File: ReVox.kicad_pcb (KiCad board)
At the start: 2 copper layers, 60.8 x 89.2 mm, 41 parts, among them CN1 EXPANSION_PORT, U1 GAL20V8, U2 74LS273, U3 LM386

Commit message: RIP
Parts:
- removed C6: 100n, Capacitor_THT:C_Disc_D7.0mm_W2.5mm_P5.00mm
- added CN2: AUDIO_OUT, ReVox:AudioJack_SJ1-3525N, F.Cu at (145.3, 62.4)
- added CN3: AUDIO_OUT, ReVox:AudioJack_SJ1-3525N, F.Cu at (129.4, 62.4)
- added J1: CONN_SIGNALS, ReVox:PinHeader_2x25_P1.27mm_Vertical, F.Cu at (136.9, 135.3)
- V0: moved to B.Cu
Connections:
- CN1 pad 10: Net-(CN1-Pad10) -> /~cs0
- CN1 pad 11: Net-(CN1-Pad11) -> /~cas
- CN1 pad 12: Net-(CN1-Pad12) -> /mux
- CN1 pad 13: Net-(CN1-Pad13) -> /ba
- CN1 pad 22: Net-(CN1-Pad22) -> /aec
- CN1 pad 4: Net-(CN1-Pad4) -> /~irq
- CN1 pad 6: Net-(CN1-Pad6) -> /c1hi
- CN1 pad 7: Net-(CN1-Pad7) -> /c2lo
- CN1 pad 8: Net-(CN1-Pad8) -> /c2hi
- CN1 pad 9: Net-(CN1-Pad9) -> /~cs1
- CN1 pad AA: Net-(CN1-PadAA) -> /aa
- CN1 pad B: Net-(CN1-PadB) -> /c1lo
- CN1 pad BB: Net-(CN1-PadBB) -> /bb
- CN1 pad D: Net-(CN1-PadD) -> /~ras
- CN1 pad E: Net-(CN1-PadE) -> /phi0
- CN1 pad Z: Net-(CN1-PadZ) -> /z
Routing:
- net +5V: track 0.00 -> 58.5 mm
- net /a9: track 0.00 -> 22.9 mm
- net /a10: track 0.00 -> 20.7 mm
- net /a11: track 0.00 -> 19.7 mm
- net /a12: track 0.00 -> 18.8 mm
- net /a15: track 0.00 -> 18.3 mm
- net /a14: track 0.00 -> 18.3 mm
- net /a13: track 0.00 -> 18.1 mm
- net /phi2: track 0.00 -> 17.0 mm
- net /~reset: track 0.00 -> 16.1 mm
- net /~ras: track 0.00 -> 15.7 mm
- net /c1lo: track 0.00 -> 15.5 mm
- net /phi0: track 0.00 -> 15.0 mm
- net /ext_audio: track 0.00 -> 13.5 mm
- net /~irq: track 0.00 -> 13.0 mm
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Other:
- net class Default: trace_width 0.25 -> 0.2
- board text added: "V1"
- board text removed: "V2"

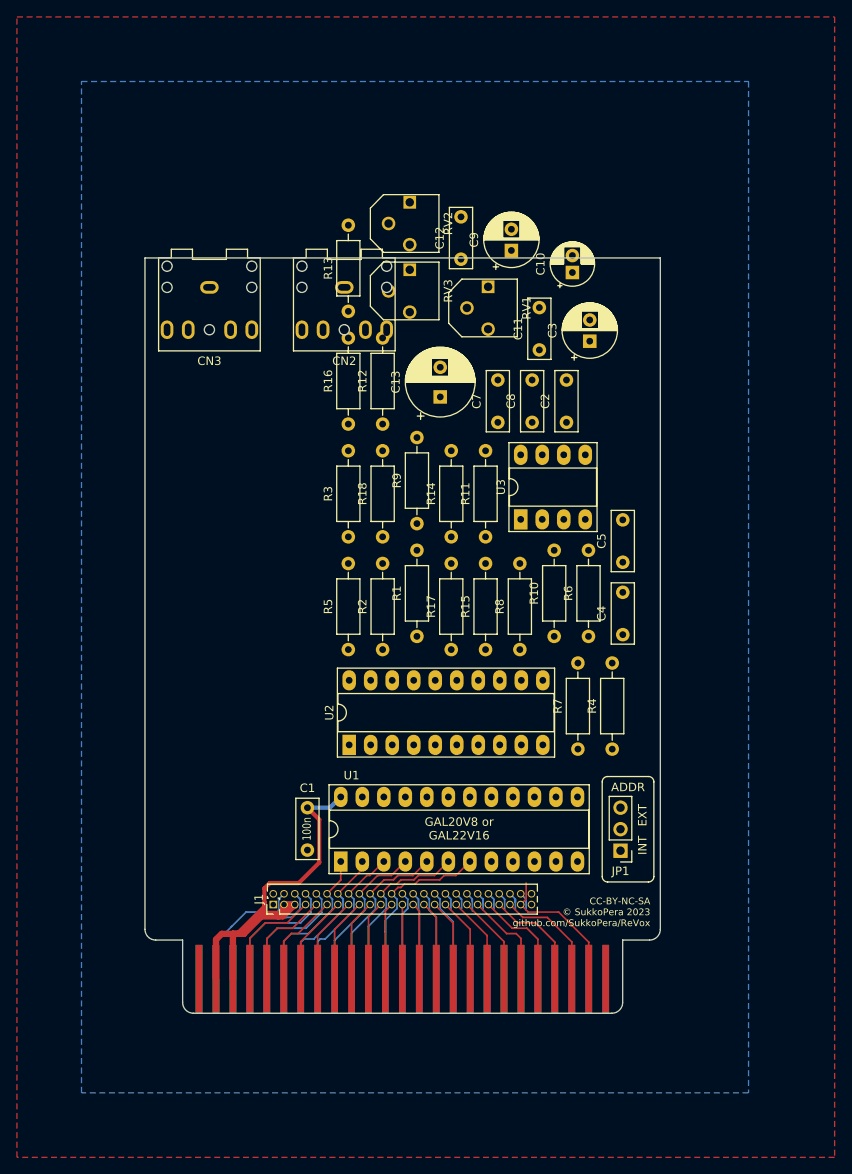
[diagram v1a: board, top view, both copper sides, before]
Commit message: First routing pass completed
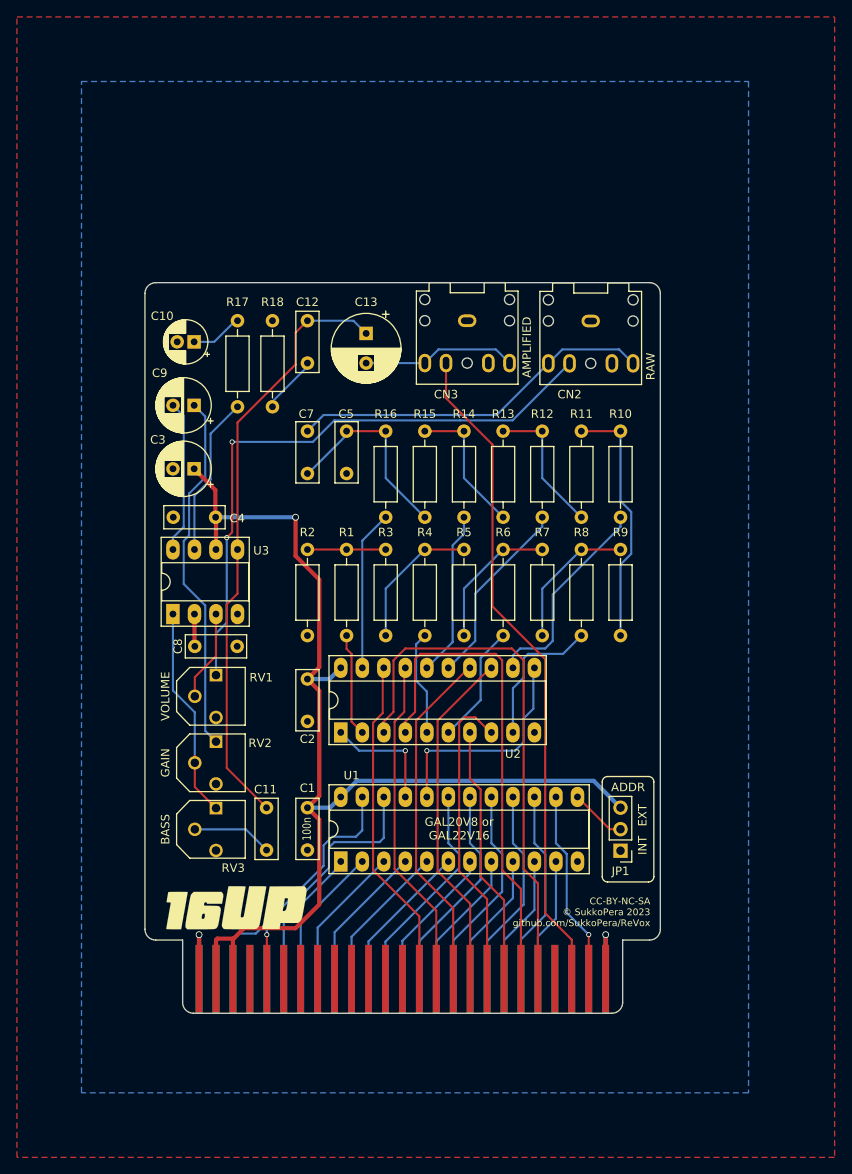
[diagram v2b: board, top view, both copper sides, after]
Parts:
- removed J1: CONN_SIGNALS, ReVox:PinHeader_2x25_P1.27mm_Vertical
- V0: moved to F.Cu
- moved RV2 67.6 mm to (128.9, 118.5)
- moved RV3 67.5 mm to (128.9, 126.4)
- moved C11 62.9 mm to (136.1, 123.8), turned to 270 degrees
- moved RV1 56.0 mm to (128.9, 110.7)
- moved C4 50.0 mm to (130.1, 89.5), turned to 180 degrees
- moved C3 49.1 mm to (127.6, 83.8), turned to 180 degrees
- moved R17 46.3 mm to (132.7, 66.3), turned to 270 degrees
- moved C10 45.4 mm to (127.6, 68.8), turned to 180 degrees
- moved C8 43.7 mm to (132.7, 104.8), turned to 180 degrees
- moved C2 43.0 mm to (141.0, 108.6), turned to 270 degrees
- moved U3 42.5 mm to (125.1, 101.0)
- moved C9 41.7 mm to (127.6, 76.3), turned to 180 degrees
- moved C5 34.2 mm to (145.6, 84.4)
- moved CN3 30.7 mm to (159.8, 66.3)
- moved R13 30.4 mm to (164.1, 89.5)
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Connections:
- C8 pad 2: Net-(C8-Pad2) -> GND
- U1 pad 10: /a6 -> /a2
- U1 pad 11: /a5 -> /a0
- U1 pad 13: /a4 -> Net-(JP1-Pad2)
- U1 pad 14: Net-(JP1-Pad2) -> /phi2
- U1 pad 15: /a3 -> /a1
- U1 pad 16: /a2 -> /a3
- U1 pad 17: /a1 -> /a5
- U1 pad 18: /a0 -> /a7
- U1 pad 19: /~reset -> /a9
- U1 pad 20: /r_~w -> /latch_clk
- U1 pad 22: /latch_clk -> /r_~w
- U1 pad 23: /phi2 -> /~reset
- U1 pad 7: /a9 -> /a8
- U1 pad 8: /a8 -> /a6
- U1 pad 9: /a7 -> /a4
- U3 pad 2: Net-(C8-Pad2) -> GND
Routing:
- net +5V: track 58.5 -> 136.3 mm, vias 0 -> 1
- net /amplifier_in: track 0.00 -> 72.0 mm, vias 0 -> 2
- net Net-(C11-Pad1): track 0.00 -> 70.9 mm
- net /ext_audio: track 13.5 -> 79.4 mm
- net /d0: track 12.2 -> 63.8 mm
- net /d1: track 11.5 -> 58.5 mm
- net /analog_audio: track 0.00 -> 43.1 mm
- net Net-(C9-Pad1): track 0.00 -> 42.9 mm
- net /d5: track 9.67 -> 41.1 mm
- net /d4: track 9.97 -> 40.9 mm
- net /d7: track 9.07 -> 39.4 mm
- net /d6: track 9.37 -> 39.2 mm
- net Net-(R10-Pad2): track 0.00 -> 29.8 mm
- net /latch_clk: track 0.00 -> 26.5 mm, vias 0 -> 1
- net /d3: track 10.3 -> 36.3 mm
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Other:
- board size 60.8 x 89.2 mm -> 60.8 x 86.2 mm
- net class Default: trace_width 0.2 -> 0.25
- board text added: "AMPLIFIED"
- board text added: "BASS"
- board text added: "GAIN"
- board text added: "RAW"
- board text added: "VOLUME"

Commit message: Refinements
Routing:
- net Net-(RV2-Pad2): track 25.8 -> 32.5 mm
- net Net-(C11-Pad1): track 70.9 -> 73.6 mm
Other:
- outline, holes or cut-outs redrawn
- board text added: "2R"
- board text added: "R"

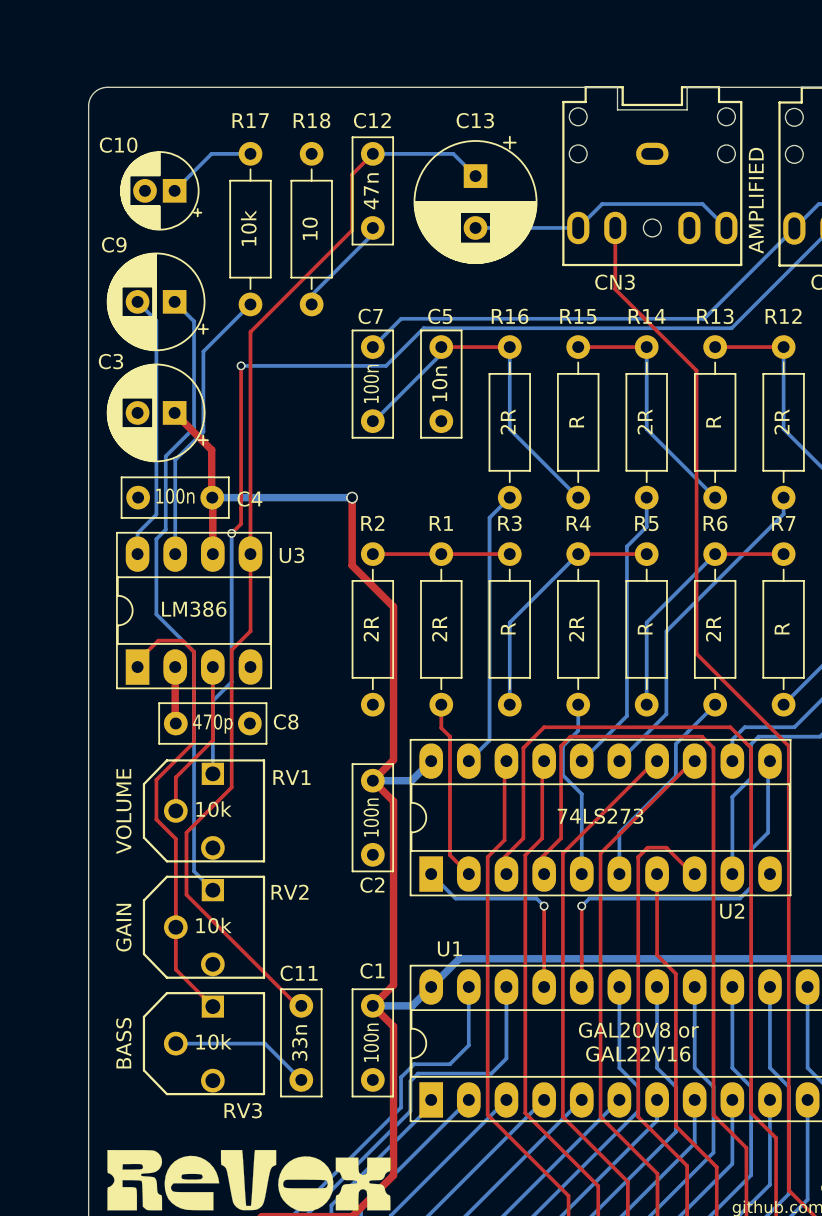
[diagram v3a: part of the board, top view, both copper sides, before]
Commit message: Move pots up, so that they remain accessible while the board is plugged into the machine
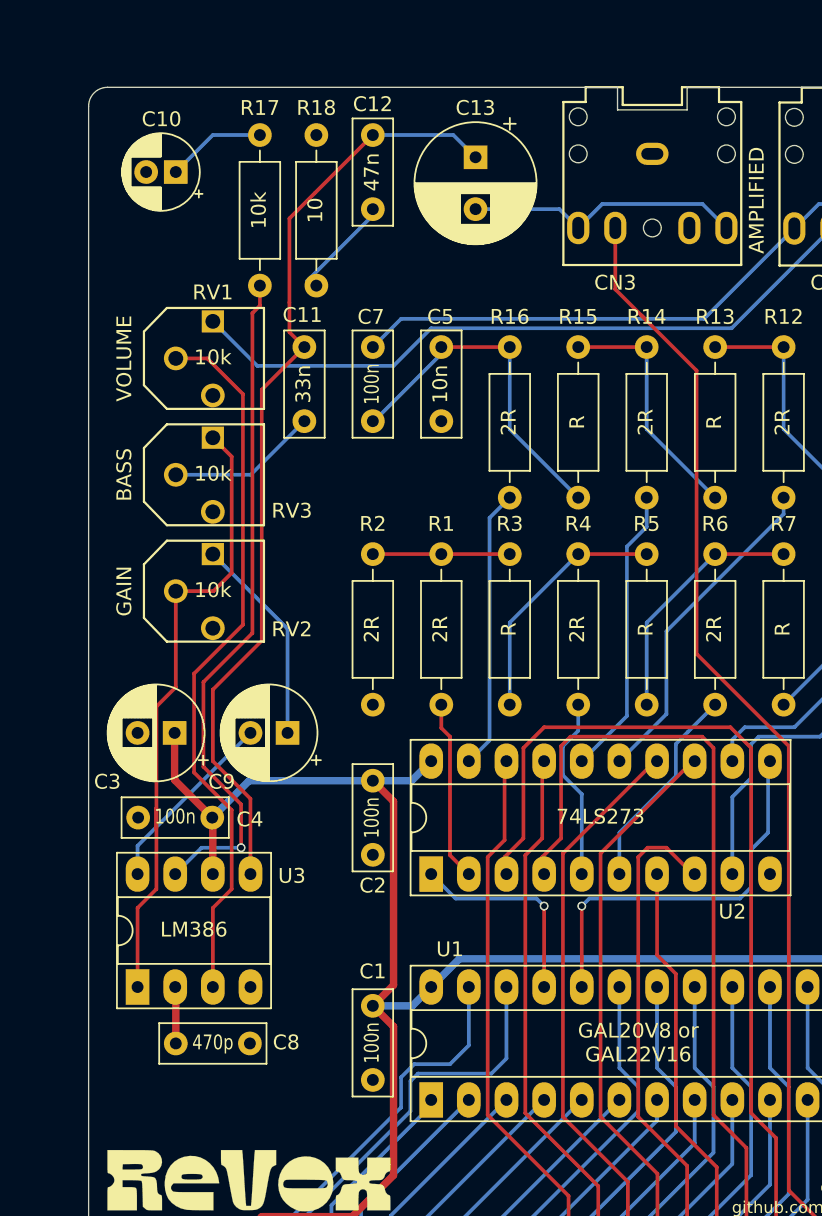
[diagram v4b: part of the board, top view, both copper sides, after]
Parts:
- moved C11 44.5 mm to (136.4, 79.4)
- moved RV3 38.4 mm to (128.9, 88.0)
- moved RV1 30.5 mm to (128.9, 80.1)
- moved C9 30.1 mm to (135.2, 105.4)
- moved RV2 22.7 mm to (128.9, 95.8)
- moved C3 21.6 mm to (127.6, 105.4)
- moved C4 21.6 mm to (130.1, 111.1)
- moved U3 21.6 mm to (125.1, 122.6)
- moved C8 21.6 mm to (132.7, 126.4)
- moved R17 1.42 mm to (133.3, 65.1)
- moved R18 1.31 mm to (137.2, 65.1)
- moved C10 1.27 mm to (127.7, 67.6)
- moved C12 1.27 mm to (141.0, 65.1)
- moved C13 1.27 mm to (147.9, 66.6)
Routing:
- net Net-(RV1-Pad2): track 10.7 -> 48.5 mm
- net Net-(C9-Pad1): track 42.9 -> 14.2 mm
- net Net-(R17-Pad2): track 19.0 -> 45.7 mm, vias 0 -> 1
- net /amplifier_in: track 72.0 -> 46.8 mm, vias 2 -> 0
- net +5V: track 136.3 -> 117.9 mm, vias 1 -> 0
- net Net-(RV2-Pad2): track 32.5 -> 43.1 mm
- net Net-(C11-Pad1): track 73.6 -> 63.8 mm
- net Net-(C9-Pad2): track 18.1 -> 12.7 mm
- net Net-(C11-Pad2): track 9.48 -> 10.2 mm
- net Net-(C10-Pad1): track 6.15 -> 6.71 mm
- net /amplified_audio: track 18.3 -> 18.8 mm

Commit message: Tidy up
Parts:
- moved C12 19.9 mm to (136.4, 84.4), turned to 90 degrees
- moved C11 14.0 mm to (136.4, 93.3)
- moved C10 3.96 mm to (131.1, 69.5)
- moved R18 3.81 mm to (141.0, 65.1)
- moved R17 3.00 mm to (136.4, 65.1)
- moved C13 1.27 mm to (147.9, 67.8)
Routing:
- net Net-(C11-Pad2): track 10.2 -> 15.0 mm
- net Net-(C11-Pad1): track 63.8 -> 61.5 mm
- net Net-(R17-Pad2): track 45.7 -> 47.0 mm
- net Net-(C12-Pad2): track 7.00 -> 6.34 mm
- net /amplified_audio: track 18.8 -> 18.2 mm

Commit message: Final touches
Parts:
- moved RV1 0.77 mm to (128.9, 79.4)
- moved V0 0.57 mm to (132.6, 136.2)
- moved RV3 0.36 mm to (128.9, 87.6)
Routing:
- net Net-(RV1-Pad2): track 48.5 -> 49.7 mm
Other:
- board text added: "CC-BY-NC-SA © SukkoPera 2023 Based on work by Yeo Kheng Meng github.com/SukkoPera/ReVox"
- board text removed: "CC-BY-NC-SA © SukkoPera 2023 github.com/SukkoPera/ReVox"
- board text removed: "THANKS TO ALL THE FOLKS AT THE PLUS/4 WORLD FORUM!"

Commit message: Final touches on silkscreen
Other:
- board text added: "74LS273 or 74LS373? WE'LL SEE!"
- board text added: "A"
- board text added: "B"
- board text removed: "ADDR"
- board text removed: "EXT"
- board text removed: "INT"

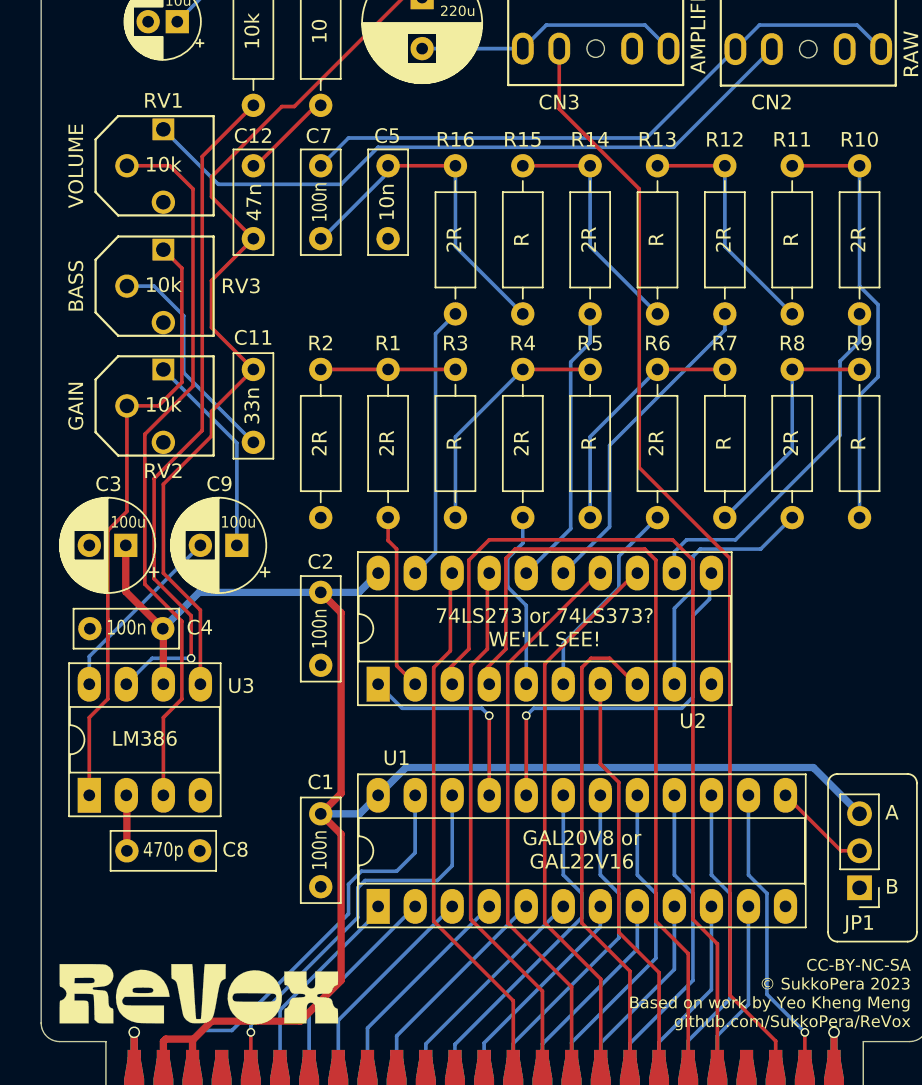
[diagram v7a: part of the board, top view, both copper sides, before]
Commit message: Shuffle some things around so that GAL20 is usable too
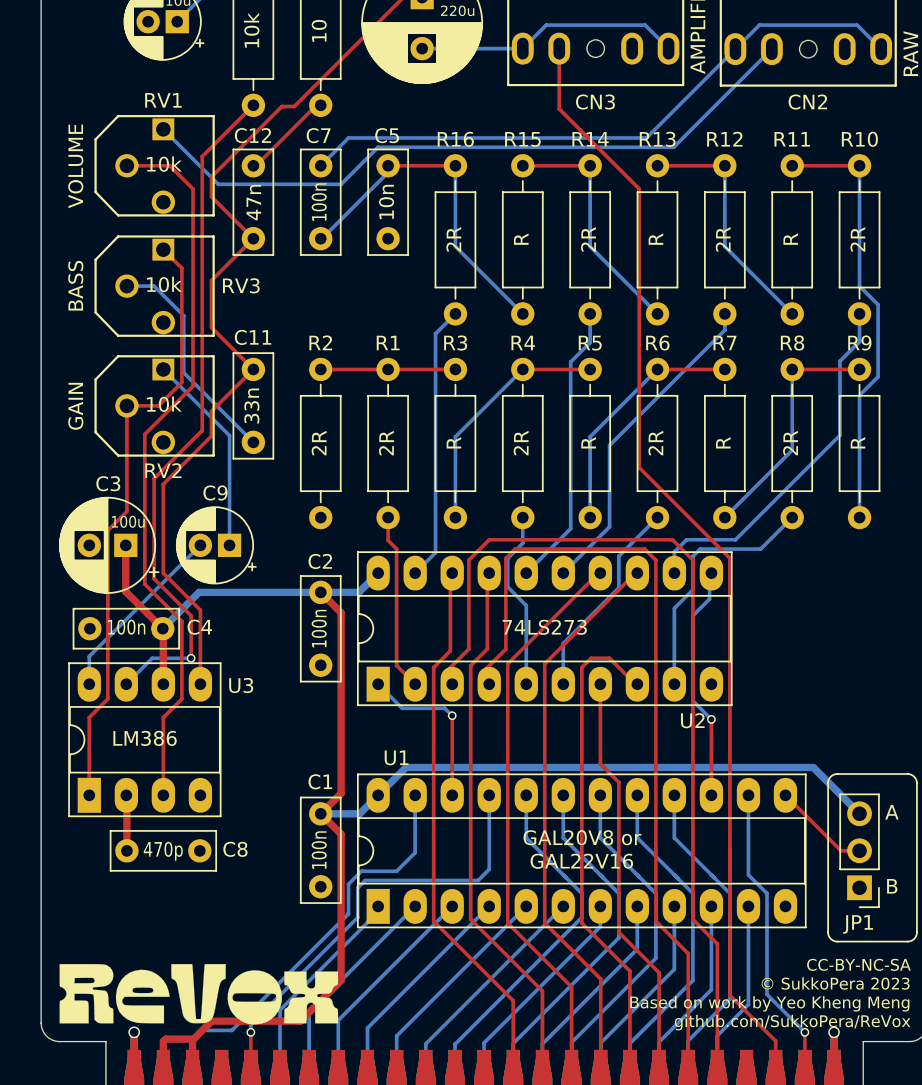
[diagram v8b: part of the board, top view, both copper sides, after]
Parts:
- C9: value 100u -> 10u; footprint Capacitor_THT:CP_Radial_D6.3mm_P2.50mm -> Capacitor_THT:CP_Radial_D5.0mm_P2.00mm
- moved C9 0.50 mm to (134.7, 105.4)
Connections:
- U1 pad 15: /a1 -> /latch_clk
- U1 pad 16: /a3 -> /a1
- U1 pad 17: /a5 -> /a3
- U1 pad 18: /a7 -> /a5
- U1 pad 19: /a9 -> /a7
- U1 pad 20: /latch_clk -> /a9
- U1 pad 21: /latch_clear -> /r_~w
- U1 pad 22: /r_~w -> /latch_clear
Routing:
- net /latch_clk: track 26.4 -> 16.2 mm
- net /ext_audio: track 79.4 -> 83.6 mm
- net /r_~w: track 30.1 -> 32.8 mm
- net /latch_clear: track 14.0 -> 11.4 mm
- net /a3: track 23.8 -> 25.2 mm
- net /a9: track 25.6 -> 26.9 mm
- net /a7: track 25.0 -> 26.3 mm
- net /a1: track 23.2 -> 24.5 mm
- net /a5: track 24.4 -> 25.6 mm
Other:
- board text removed: "74LS273 or 74LS373? WE'LL SEE!"
